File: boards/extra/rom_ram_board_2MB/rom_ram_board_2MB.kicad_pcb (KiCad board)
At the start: 2 copper layers, 95.2 x 95.2 mm, 33 parts, among them J1 Exp. Conn. A, J2 Power, U1 74LS04, U10 AS6C4008-55PCN, U11 74LS670, U2 74LS30, U3 74LS32, U4 74LS670, U5 SST39SF040, U6 74LS244, U7 AS6C4008-55PCN, U8 74LS139, U9 AS6C4008-55PCN

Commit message: * Working on new powerdistribution method.
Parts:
- removed J2: Power, Connector_IDC:IDC-Header_2x10_P2.54mm_Horizontal
- added J3: Power, footprints:TE_171826-4, F.Cu at (120.1, 105.2)
- R1: value 470 -> 1k
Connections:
- C1 pad 1: /+5V3 -> /+5V
- C10 pad 1: /+5V3 -> /+5V
- C11 pad 1: /+5V3 -> /+5V
- C2 pad 1: /+5V3 -> /+5V
- C3 pad 1: /+5V3 -> /+5V
- C4 pad 1: /+5V3 -> /+5V
- C5 pad 1: /+5V3 -> /+5V
- C6 pad 1: /+5V3 -> /+5V
- C7 pad 1: /+5V3 -> /+5V
- C8 pad 1: /+5V3 -> /+5V
- C9 pad 1: /+5V3 -> /+5V
- CP1 pad 1: /+5V3 -> /+5V
- CP2 pad 1: /+5V3 -> /+5V
- R1 pad 1: /+5V3 -> /+5V
- U1 pad 14: /+5V3 -> /+5V
- U10 pad 32: /+5V3 -> /+5V
- U11 pad 16: /+5V3 -> /+5V
- U2 pad 14: /+5V3 -> /+5V
- U3 pad 14: /+5V3 -> /+5V
- U4 pad 16: /+5V3 -> /+5V
- U5 pad 31: /+5V3 -> /+5V
- U5 pad 32: /+5V3 -> /+5V
- U6 pad 20: /+5V3 -> /+5V
- U7 pad 32: /+5V3 -> /+5V
- U8 pad 16: /+5V3 -> /+5V
- U9 pad 32: /+5V3 -> /+5V
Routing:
- net /+5V: track 0.00 -> 389.2 mm
- net /+5V3: track 359.3 -> 0.00 mm
- net /GND: track 54.0 -> 37.5 mm, vias 157 -> 159
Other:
- board text added: "+5V"
- board text added: "GND"
- board text added: "NC"

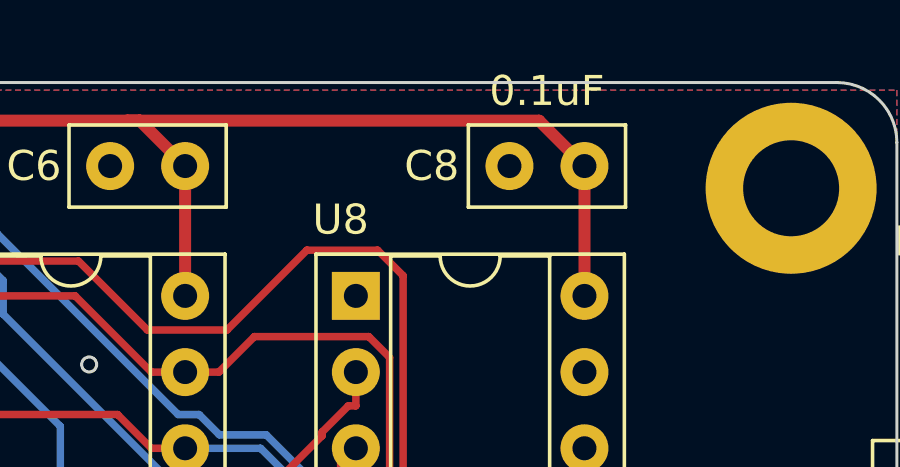
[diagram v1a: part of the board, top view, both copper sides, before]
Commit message: Added expansion connector C and designed some new boards around it.
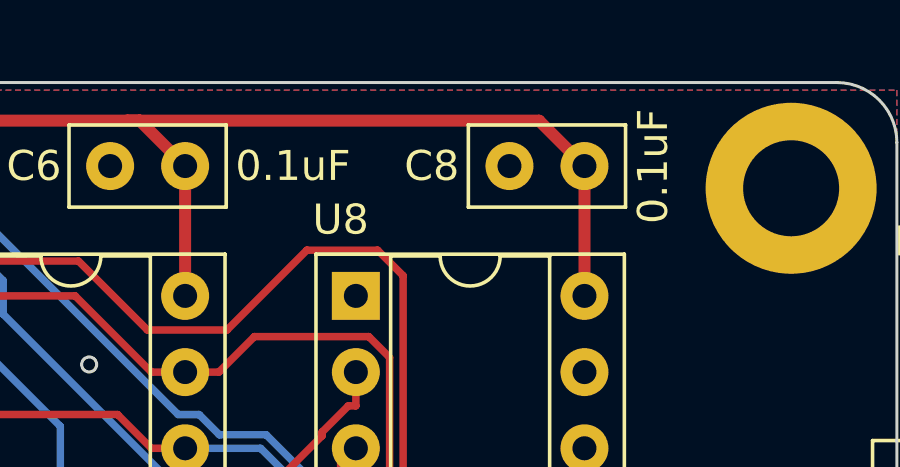
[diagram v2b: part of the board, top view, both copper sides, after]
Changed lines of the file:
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@@
         (effects (font (size 1 1) (thickness 0.15)))
     )
-    (fp_text value "0.1uF" (at -3.596 0) (layer "F.Fab")
+    (fp_text value "0.1uF" (at -3.596 0) (layer "F.SilkS")
         (effects (font (size 1 1) (thickness 0.15)))
     )
@@
         (effects (font (size 1 1) (thickness 0.15)))
     )
-    (fp_text value "0.1uF" (at 1.25 2.5) (layer "F.SilkS")
-        (effects (font (size 1 1) (thickness 0.15)))
-    )
+    (fp_text value "0.1uF" (at -2.286 -0.01 90) (layer "F.SilkS")
+        (effects (font (size 1 1) (thickness 0.15)))
+    )
